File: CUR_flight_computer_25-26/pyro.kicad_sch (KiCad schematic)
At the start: 22 parts, among them J10 PYRO, J11 PYRO, J8 PYRO, J9 PYRO, U12 BUK9K25-40RAX, U13 BUK9K25-40RAX

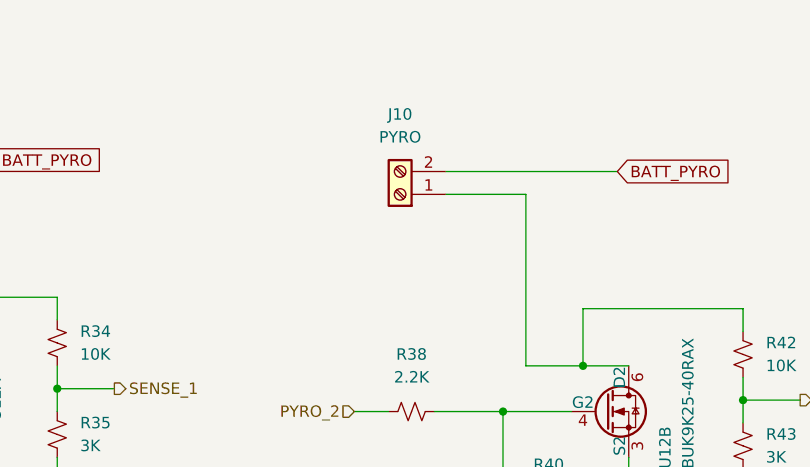
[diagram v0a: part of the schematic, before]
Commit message: Improve pyro routing
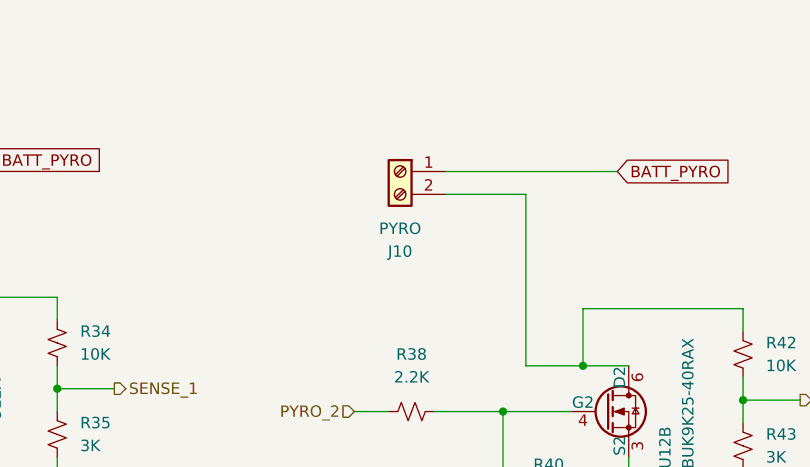
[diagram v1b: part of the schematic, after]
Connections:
- net BATT_PYRO: now also J10.1 (Pin_1); no longer J10.2 (Pin_2)
- net at R42.1, U12.6 (D2): now also J10.2 (Pin_2); no longer J10.1 (Pin_1)
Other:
- moved on the sheet: J10
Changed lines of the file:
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@@
 	(symbol
 		(lib_id "Connector:Screw_Terminal_01x02")
-		(at 125.73 46.99 180)
+		(at 125.73 44.45 0)
+		(mirror y)
 		(unit 1)
 		(exclude_from_sim no)
@@
 		(on_board yes)
 		(dnp no)
-		(fields_autoplaced yes)
 		(property "Reference" "J10"
-			(at 125.73 38.1 0)
+			(at 125.73 53.34 0)
 			(effects
 				(font
@@
 		)
 		(property "Value" "PYRO"
-			(at 125.73 40.64 0)
+			(at 125.73 50.8 0)
 			(effects
 				(font
@@
 		)
 		(property "Footprint" "Terminal_SAMESKY_TB0011-350-02GR:SAMESKY_TB0011-350-02GR"
-			(at 125.73 46.99 0)
+			(at 125.73 44.45 0)
 			(effects
 				(font
@@
 		)
 		(property "Datasheet" "~"
-			(at 125.73 46.99 0)
+			(at 125.73 44.45 0)
 			(effects
 				(font
@@
 		)
 		(property "Description" "Generic screw terminal, single row, 01x02, script generated (kicad-library-utils/schlib/autogen/connector/)"
-			(at 125.73 46.99 0)
+			(at 125.73 44.45 0)
 			(effects
 				(font

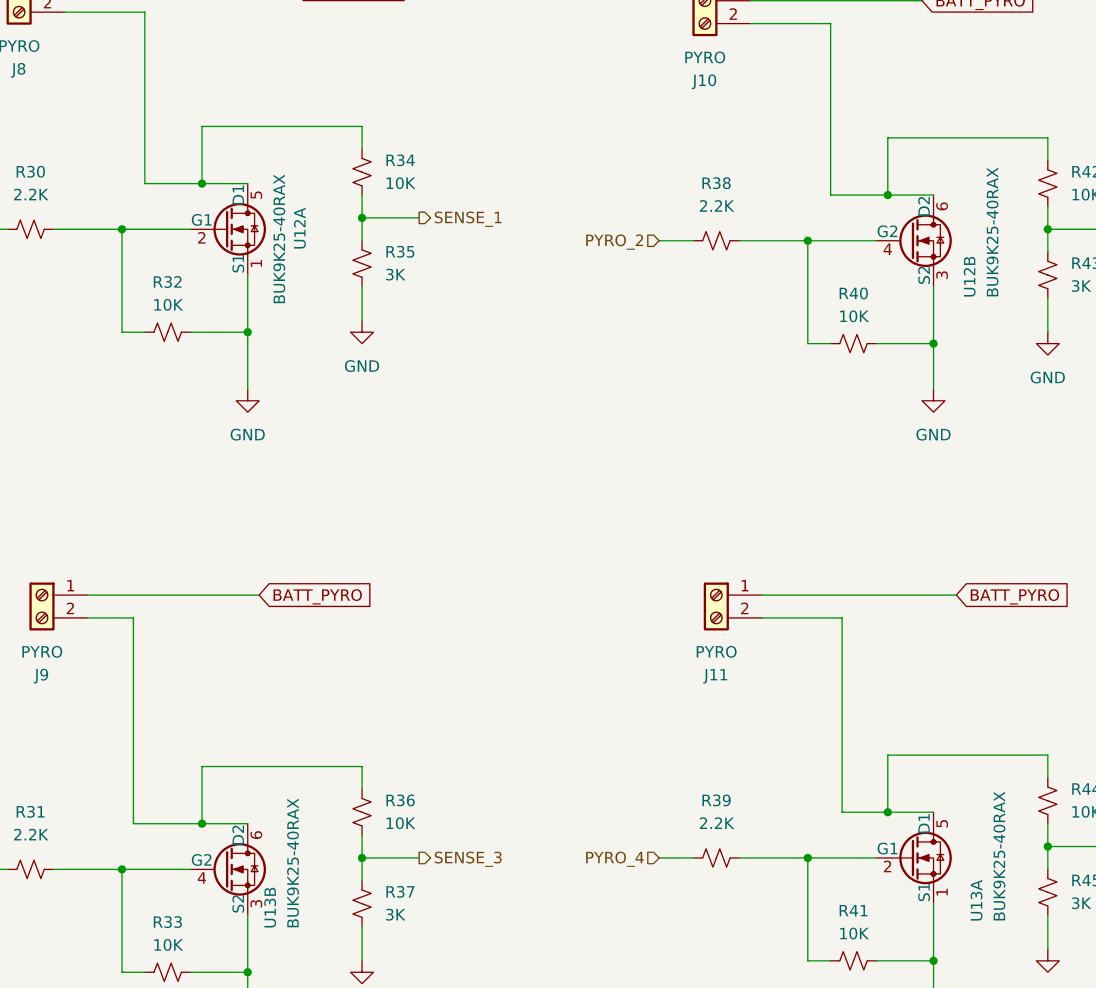
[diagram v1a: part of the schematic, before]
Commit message: Finish routing pyro
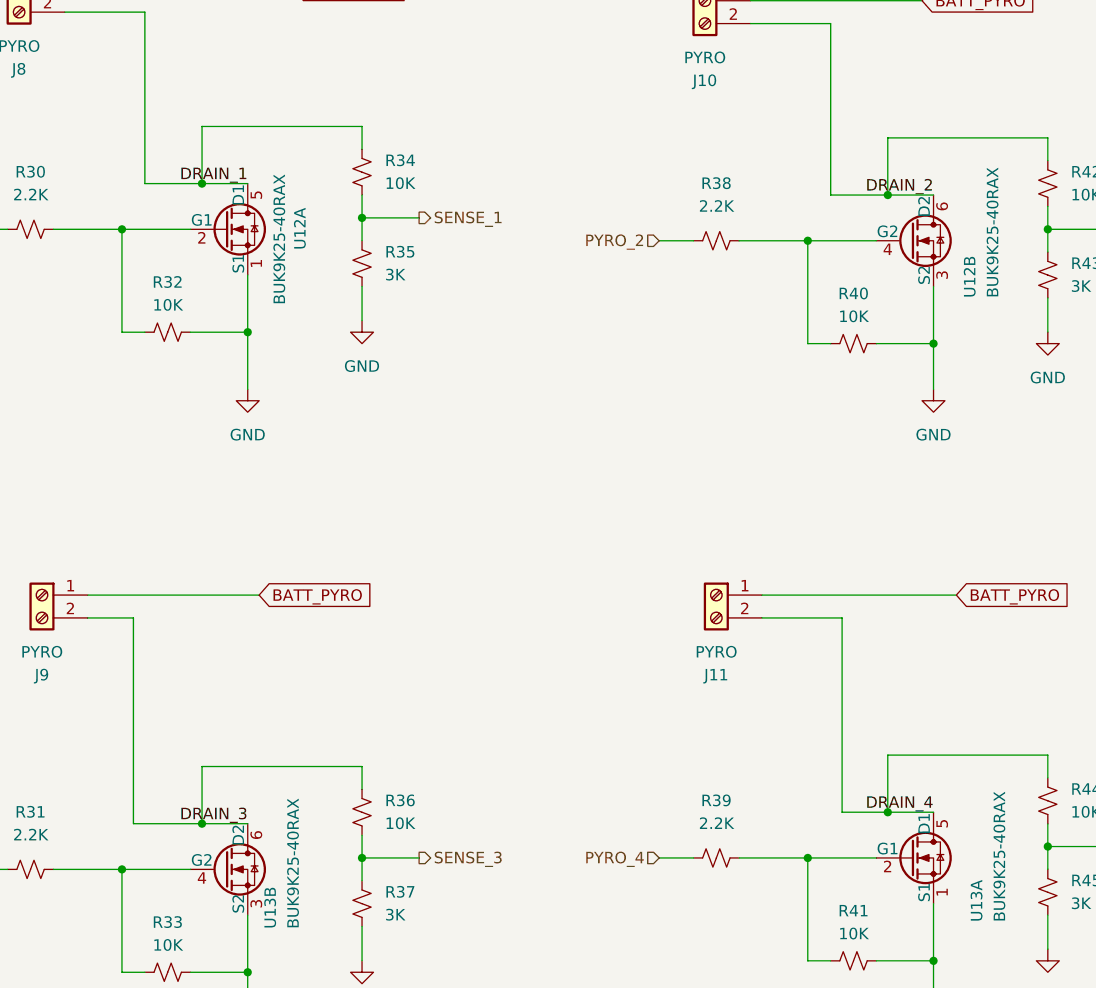
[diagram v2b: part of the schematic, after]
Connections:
- net DRAIN_4: now reaches J11.2 (Pin_2), R44.1, U13.5 (D1)
- net DRAIN_3: now reaches J9.2 (Pin_2), R36.1, U13.6 (D2)
- net DRAIN_1: now reaches J8.2 (Pin_2), R34.1, U12.5 (D1)
- net DRAIN_2: now reaches J10.2 (Pin_2), R42.1, U12.6 (D2)
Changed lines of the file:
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@@
+		)
+	)
+	(label "DRAIN_1"
+		(at 74.93 64.77 180)
+		(effects
+			(font
+				(size 1.27 1.27)
+			)
+			(justify right bottom)
+		)
+	)
+	(label "DRAIN_3"
+		(at 74.93 135.89 180)
+		(effects
+			(font
+				(size 1.27 1.27)
+			)
+			(justify right bottom)
+		)
+	)
+	(label "DRAIN_4"
+		(at 151.13 134.62 180)
+		(effects
+			(font
+				(size 1.27 1.27)
+			)
+			(justify right bottom)
+		)
+	)
+	(label "DRAIN_2"
+		(at 151.13 66.04 180)
+		(effects
+			(font
+				(size 1.27 1.27)
+			)
+			(justify right bottom)
 		)
 	)

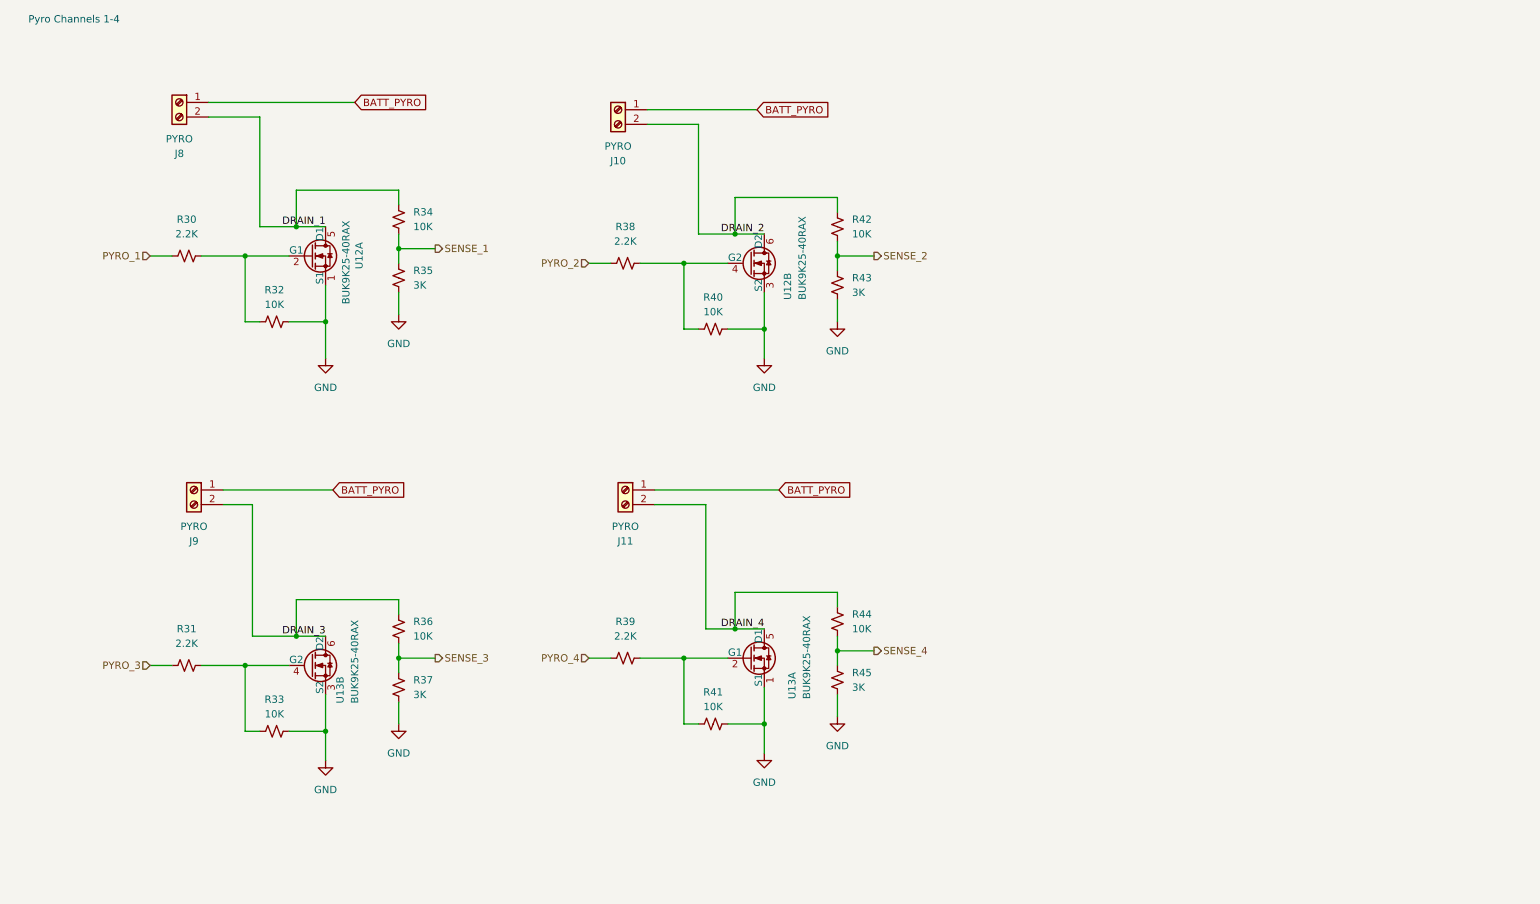
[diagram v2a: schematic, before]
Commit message: Add MPNs for ICs
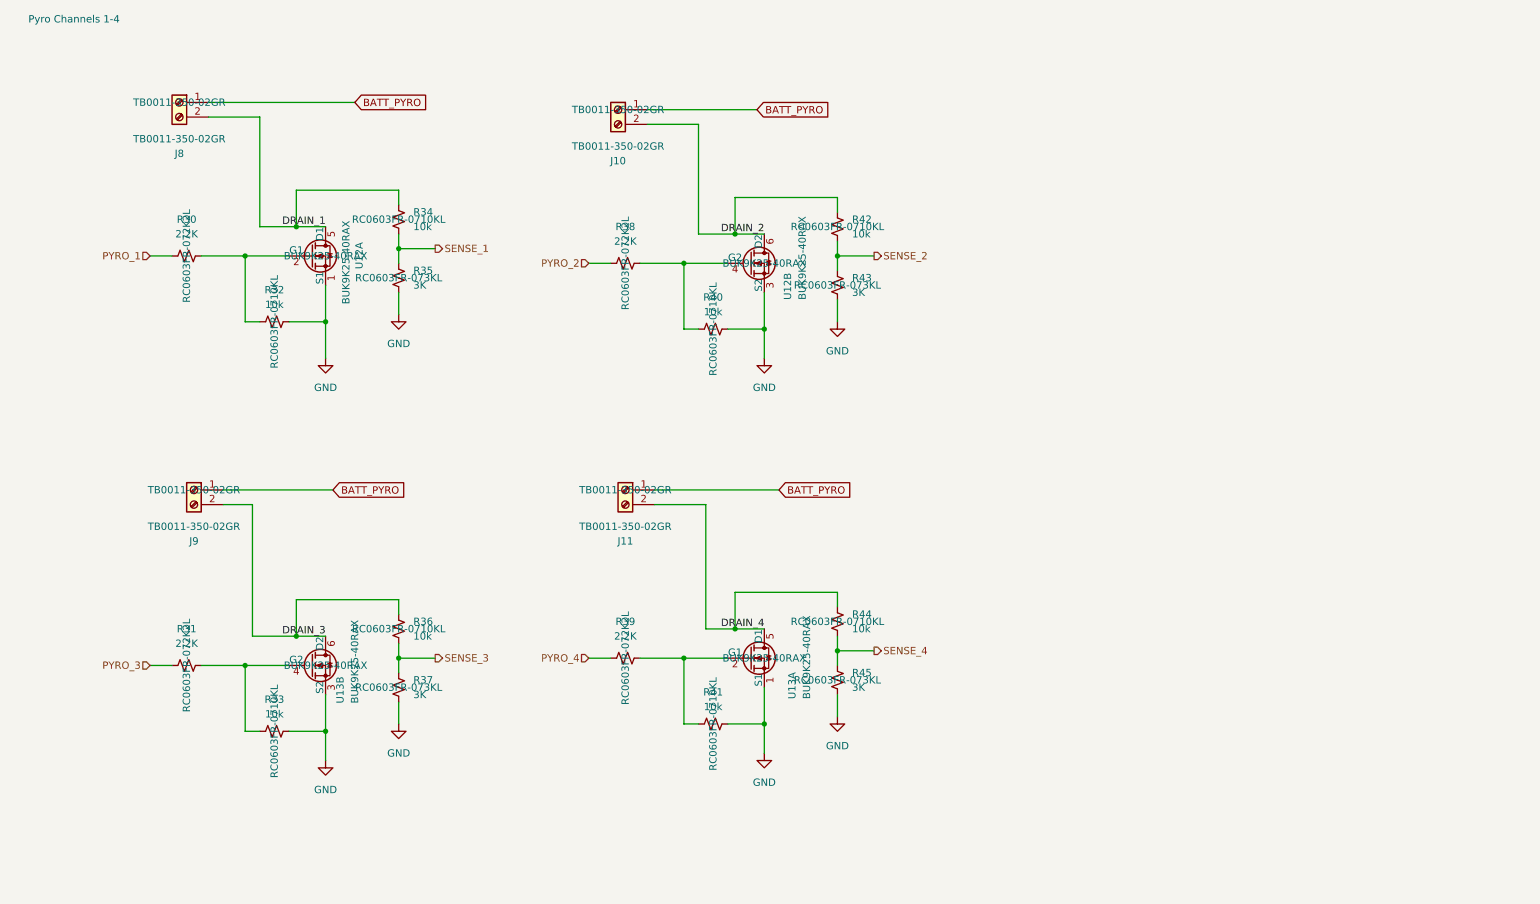
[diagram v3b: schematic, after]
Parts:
- J10, J11, J8, J9: value PYRO -> TB0011-350-02GR; MPN (none) -> TB0011-350-02GR
- R30, R31, R38, R39: MPN (none) -> RC0603FR-072K2L
- R32, R33, R34, R36, R40, R41, R42, R44: value 10K -> 10k; MPN (none) -> RC0603FR-0710KL
- R35, R37, R43, R45: MPN (none) -> RC0603FR-073KL
- U12, U13: MPN (none) -> BUK9K25-40RAX
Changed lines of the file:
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@@
+			)
+		)
+		(property "MPN" "BUK9K25-40RAX"
+			(at 151.13 139.7 0)
+			(effects
+				(font
+					(size 1.27 1.27)
+				)
 			)
 		)
@@
 			)
 		)
-		(property "Value" "10K"
+		(property "Value" "10k"
 			(at 66.04 78.2909 90)
 			(effects
@@
 				)
 				(hide yes)
+			)
+		)
+		(property "MPN" "RC0603FR-0710KL"
+			(at 66.04 81.28 0)
+			(effects
+				(font
+					(size 1.27 1.27)
+				)
 			)
 		)
@@
 			)
 		)
-		(property "Value" "PYRO"
+		(property "Value" "TB0011-350-02GR"
 			(at 52.07 116.84 0)
 			(effects
@@
 			)
 		)
+		(property "MPN" "TB0011-350-02GR"
+			(at 52.07 110.49 0)
+			(effects
+				(font
+					(size 1.27 1.27)
+				)
+			)
+		)
 		(pin "1"
 		)
@@
 			)
 		)
-		(property "Value" "10K"
+		(property "Value" "10k"
 			(at 166.37 134.6199 0)
 			(effects
@@
 				)
 				(hide yes)
+			)
+		)
+		(property "MPN" "RC0603FR-0710KL"
+			(at 163.83 133.35 0)
+			(effects
+				(font
+					(size 1.27 1.27)
+				)
 			)
 		)
@@
 			)
 		)
+		(property "MPN" "BUK9K25-40RAX"
+			(at 74.93 140.97 0)
+			(effects
+				(font
+					(size 1.27 1.27)
+				)
+			)
+		)
 		(pin "4"
 		)
@@
 			)
 		)
+		(property "MPN" "BUK9K25-40RAX"
+			(at 74.93 69.85 0)
+			(effects
+				(font
+					(size 1.27 1.27)
+				)
+			)
+		)
 		(pin "4"
 		)
@@
 			)
 		)
-		(property "Value" "10K"
+		(property "Value" "10k"
 			(at 90.17 64.7699 0)
 			(effects
@@
 			)
 		)
+		(property "MPN" "RC0603FR-0710KL"
+			(at 87.63 63.5 0)
+			(effects
+				(font
+					(size 1.27 1.27)
+				)
+			)
+		)
 		(pin "1"
 		)
@@
 			)
 		)
-		(property "Value" "10K"
+		(property "Value" "10k"
 			(at 90.17 135.8899 0)
 			(effects
@@
 			)
 		)
+		(property "MPN" "RC0603FR-0710KL"
+			(at 87.63 134.62 0)
+			(effects
+				(font
+					(size 1.27 1.27)
+				)
+			)
+		)
 		(pin "1"
 		)
@@
 			)
 		)
+		(property "MPN" "RC0603FR-073KL"
+			(at 87.63 144.78 0)
+			(effects
+				(font
+					(size 1.27 1.27)
+				)
+			)
+		)
 		(pin "1"
 		)
@@
 			)
 		)
+		(property "MPN" "RC0603FR-072K2L"
+			(at 127 139.7 0)
+			(effects
+				(font
+					(size 1.27 1.27)
+				)
+			)
+		)
 		(pin "1"
 		)
@@
 			)
 		)
+		(property "MPN" "RC0603FR-073KL"
+			(at 163.83 74.93 0)
+			(effects
+				(font
+					(size 1.27 1.27)
+				)
+			)
+		)
 		(pin "1"
 		)
@@
 			)
 		)
-		(property "Value" "10K"
+		(property "Value" "10k"
 			(at 142.24 148.1409 90)
 			(effects
@@
 			)
 		)
+		(property "MPN" "RC0603FR-0710KL"
+			(at 142.24 151.13 0)
+			(effects
+				(font
+					(size 1.27 1.27)
+				)
+			)
+		)
 		(pin "1"
 		)
@@
 			)
 		)
+		(property "MPN" "RC0603FR-072K2L"
+			(at 50.8 69.85 0)
+			(effects
+				(font
+					(size 1.27 1.27)
+				)
+			)
+		)
 		(pin "1"
 		)
@@
 			)
 		)
-		(property "Value" "10K"
+		(property "Value" "10k"
 			(at 142.24 79.5609 90)
 			(effects
@@
 				)
 				(hide yes)
+			)
+		)
+		(property "MPN" "RC0603FR-0710KL"
+			(at 142.24 82.55 0)
+			(effects
+				(font
+					(size 1.27 1.27)
+				)
 			)
 		)
@@
 			)
 		)
-		(property "Value" "PYRO"
+		(property "Value" "TB0011-350-02GR"
 			(at 49.53 49.53 0)
 			(effects
@@
 			)
 		)
+		(property "MPN" "TB0011-350-02GR"
+			(at 49.53 43.18 0)
+			(effects
+				(font
+					(size 1.27 1.27)
+				)
+			)
+		)
 		(pin "1"
 		)
@@
 				)
 				(hide yes)
+			)
+		)
+		(property "MPN" "RC0603FR-072K2L"
+			(at 127 71.12 0)
+			(effects
+				(font
+					(size 1.27 1.27)
+				)
 			)
 		)
@@
 			)
 		)
-		(property "Value" "PYRO"
+		(property "Value" "TB0011-350-02GR"
 			(at 127 116.84 0)
 			(effects
@@
 			)
 		)
+		(property "MPN" "TB0011-350-02GR"
+			(at 127 110.49 0)
+			(effects
+				(font
+					(size 1.27 1.27)
+				)
+			)
+		)
 		(pin "1"
 		)
@@
 			)
 		)
-		(property "Value" "10K"
+		(property "Value" "10k"
 			(at 166.37 66.0399 0)
 			(effects
@@
 			)
 		)
+		(property "MPN" "RC0603FR-0710KL"
+			(at 163.83 64.77 0)
+			(effects
+				(font
+					(size 1.27 1.27)
+				)
+			)
+		)
 		(pin "1"
 		)
@@
 				)
 				(hide yes)
+			)
+		)
+		(property "MPN" "RC0603FR-073KL"
+			(at 163.83 143.51 0)
+			(effects
+				(font
+					(size 1.27 1.27)
+				)
 			)
 		)
@@
 			)
 		)
-		(property "Value" "PYRO"
+		(property "Value" "TB0011-350-02GR"
 			(at 125.73 50.8 0)
 			(effects
@@
 			)
 		)
+		(property "MPN" "TB0011-350-02GR"
+			(at 125.73 44.45 0)
+			(effects
+				(font
+					(size 1.27 1.27)
+				)
+			)
+		)
 		(pin "1"
 		)
@@
 			)
 		)
+		(property "MPN" "RC0603FR-073KL"
+			(at 87.63 73.66 0)
+			(effects
+				(font
+					(size 1.27 1.27)
+				)
+			)
+		)
 		(pin "1"
 		)
@@
 				)
 				(hide yes)
+			)
+		)
+		(property "MPN" "RC0603FR-072K2L"
+			(at 50.8 140.97 0)
+			(effects
+				(font
+					(size 1.27 1.27)
+				)
 			)
 		)
@@
 			)
 		)
+		(property "MPN" "BUK9K25-40RAX"
+			(at 151.13 71.12 0)
+			(effects
+				(font
+					(size 1.27 1.27)
+				)
+			)
+		)
 		(pin "4"
 		)
@@
 			)
 		)
-		(property "Value" "10K"
+		(property "Value" "10k"
 			(at 66.04 149.4109 90)
 			(effects
@@
 			)
 		)
+		(property "MPN" "RC0603FR-0710KL"
+			(at 66.04 152.4 0)
+			(effects
+				(font
+					(size 1.27 1.27)
+				)
+			)
+		)
